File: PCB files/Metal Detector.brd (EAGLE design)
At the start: 100 x 80 mm, 93 parts, among them IC1 NE5534AD, IC2 BQ24133RGYR, IC3 LM317MBSTT3, IC4 ESP32-WROOM-32UE-N4, IC5 CP2102, IC6 LM317MBSTT3, J1 L-KLS1-TSJ3.5-013, Q1 IRF740, Q2 BC556, Q3 SI2312CDS-T1-GE3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

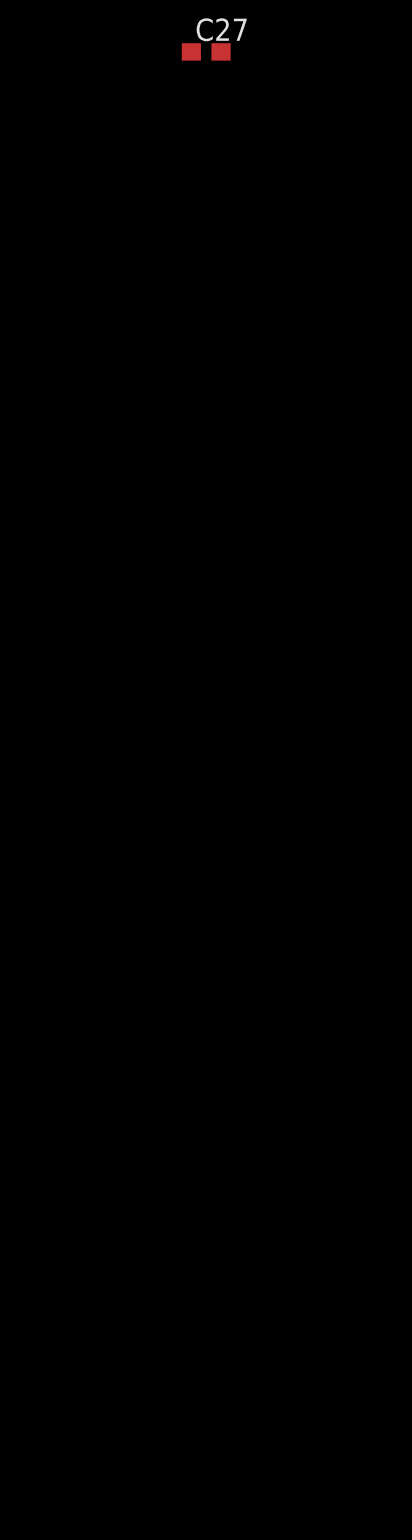
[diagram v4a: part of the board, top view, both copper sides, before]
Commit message: Add files via upload
Still designing battery charge circuit, it is almost over.
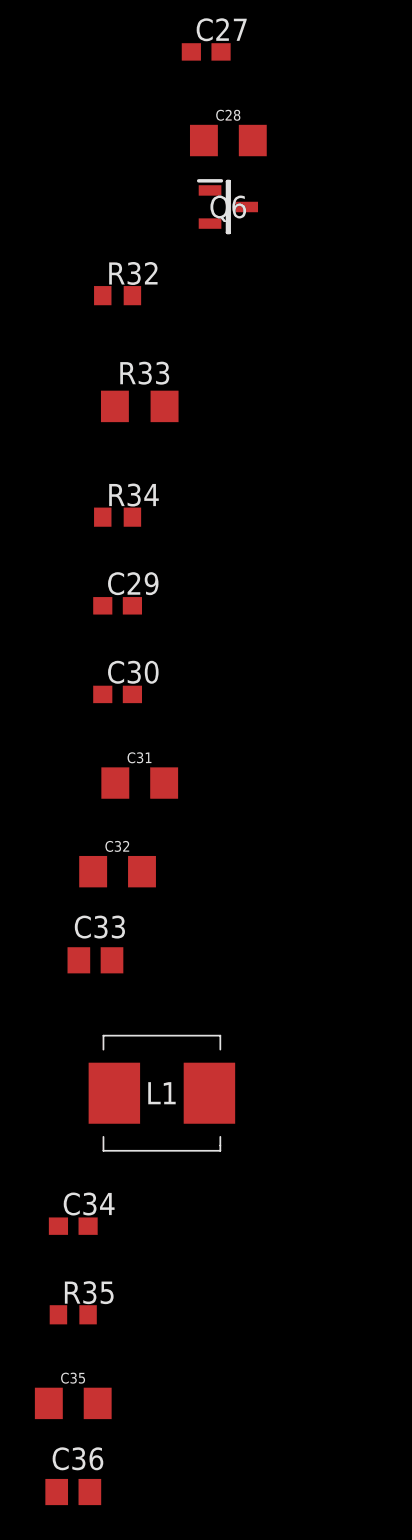
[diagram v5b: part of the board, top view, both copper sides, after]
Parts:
- added C28: 10uF/25 VDC/XR7, SparkFun-Capacitors:1206
- added C29, C30: 0.1uF, rcl:C0603
- added C31, C32, C35: 10uF/25V/XR7, SparkFun-Capacitors:1206
- added C33: 1uF/25V/XR7, rcl:C0805
- added C34: 0.047uF/50V/XR7, rcl:C0603
- added C36: 1uF/16V/XR7, rcl:C0805
- added L1: SRP7028A-3R3M, SRP7028A-3R3M:SRP7028A3R3M
- added Q6: SI2323CDS-T1-GE3, SI2323CDS-T1-GE3:SOT95P237X112-3N
- added R32: 1kΩ, rcl:R0603
- added R33: 0.01RΩ, rcl:R1206
- added R34, R35: 0Ω, rcl:R0603
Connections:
- removed net EXT_PWR_IN: C12.1, C8.1, D10.C, D12.1, D6.C, IC3.3, IC6.3, Q3.3, R15.2, R23.2, X2.2
- removed net PGND_1: IC2.22
- removed net PGND_2: IC2.23
- removed net PVCC_1: IC2.2
- removed net PVCC_2: IC2.3
- removed net SW_1: IC2.1
- removed net SW_2: IC2.24
- new net 12V_IN: D12.1, Q3.3, R15.2, R23.2, X2.2
- new net N$23: Q6.1, R32.1
- new net N$25: C34.2, R35.2
- new net PGND: IC2.22, IC2.23
- new net PVCC: IC2.2, IC2.3
- new net SW: C34.1, IC2.1, IC2.24, L1.1
- net ACP: now also Q5.3; no longer Q5.2
- net BATDRV: now also R32.2
- net BTST: now also R35.1
- net GND: now also C28.2, C30.2, C31.2, C32.2, C33.2, C35.2, C36.1
- net N$21: now also Q5.2; no longer Q5.3
- net N$24: now also C31.1, C32.1, C33.1, Q6.3, R33.2, R34.2; no longer R30.2, R31.2
- net SRN: now also C29.1, R34.1
- net SRP: now also C29.2, C30.1, L1.2, R33.1
- net VCC: now also C12.1, C28.1, C35.1, C8.1, D10.C, D6.C, IC3.3, IC6.3, Q6.2, R30.2, R31.2
- net VREF: now also C36.2

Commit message: Add files via upload
Battery Charge Circuit design process is finished but This design is unexpectedly expencive due to peripheral components.
Founded new IC and will change design for new IC. ( I'm so sorry for that : /) will be more cost effective.
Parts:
- removed C12, C8: 0.1uF, rcl:C075-052X106
- added C37: 1uF/25V/XR7, rcl:C0805
- added C38: 0.1uF/50V/XR7, rcl:C0603
- added C39, C40: 0.1uF, rcl:C2012
- added J2/BATTERY: DG128-5.0-02P-14, DG128-5.0-02P-14:DG1285002P14
- added R36, R37, R38, R39, R40, R41: 0Ω, rcl:R0603
- added R42: 30.1kΩ, rcl:R0603
- added R43: 5.23kΩ, rcl:R0603
- added U$1: 103AP-2, 130-AP2:AT-2_SMI
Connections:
- removed net AGND: IC2.25
- removed net PGND: IC2.22, IC2.23
- removed net VREF: C36.2, IC2.12
- new net N$27: C38.1, R41.2
- net ACSET: now also R38.1, R39.2
- net CELL: now also R40.2
- net GND: now also C37.2, C38.2, C39.2, C40.2, IC2.22, IC2.23, IC2.25, J2/BATTERY.2, R37.1, R39.1, R42.2, U$1.2; no longer C12.2, C8.2
- net ISET: now also R36.1, R37.2
- net N$24: now also J2/BATTERY.1
- net PVCC: now also C28.1, C35.1, Q6.2, R30.2, R31.2
- net REGN: now also C37.1
- net TS: now also R42.1, R43.2, U$1.1
- net TTC: now also R41.1
- net VCC: now also C36.2, C39.1, C40.1, IC2.12, R36.2, R38.2, R40.1, R43.1; no longer C12.1, C28.1, C35.1, C8.1, Q6.2, R30.2, R31.2

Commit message: Add files via upload
Assigned ISET adn ACSET value for selected battery
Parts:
- R36: value 0Ω -> 100kΩ
- R37: value 0Ω -> 12kΩ
- R38: value 0Ω -> 2.2Ω
- R39: value 0Ω -> 4.7Ω
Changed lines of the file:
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@@
 <attribute name="VALUE" x="-140.97" y="-520.7" size="1.27" layer="27"/>
 </element>
-<element name="R36" library="rcl" library_urn="urn:adsk.eagle:library:334" package="R0603" package3d_urn="urn:adsk.eagle:package:23555/3" value="0Ω" x="-140.97" y="-524.51" smashed="yes">
+<element name="R36" library="rcl" library_urn="urn:adsk.eagle:library:334" package="R0603" package3d_urn="urn:adsk.eagle:package:23555/3" value="100kΩ" x="-140.97" y="-524.51" smashed="yes">
 <attribute name="NAME" x="-141.605" y="-523.875" size="1.27" layer="25"/>
 <attribute name="POPULARITY" value="70" x="-140.97" y="-524.51" size="1.778" layer="27" display="off"/>
@@
 <attribute name="VALUE" x="-141.605" y="-526.415" size="1.27" layer="27"/>
 </element>
-<element name="R37" library="rcl" library_urn="urn:adsk.eagle:library:334" package="R0603" package3d_urn="urn:adsk.eagle:package:23555/3" value="0Ω" x="-140.97" y="-529.59" smashed="yes">
+<element name="R37" library="rcl" library_urn="urn:adsk.eagle:library:334" package="R0603" package3d_urn="urn:adsk.eagle:package:23555/3" value="12kΩ" x="-140.97" y="-529.59" smashed="yes">
 <attribute name="NAME" x="-141.605" y="-528.955" size="1.27" layer="25"/>
 <attribute name="POPULARITY" value="70" x="-140.97" y="-529.59" size="1.778" layer="27" display="off"/>
@@
 <attribute name="VALUE" x="-141.605" y="-531.495" size="1.27" layer="27"/>
 </element>
-<element name="R38" library="rcl" library_urn="urn:adsk.eagle:library:334" package="R0603" package3d_urn="urn:adsk.eagle:package:23555/3" value="0Ω" x="-140.97" y="-534.67" smashed="yes">
+<element name="R38" library="rcl" library_urn="urn:adsk.eagle:library:334" package="R0603" package3d_urn="urn:adsk.eagle:package:23555/3" value="2.2Ω" x="-140.97" y="-534.67" smashed="yes">
 <attribute name="NAME" x="-141.605" y="-534.035" size="1.27" layer="25"/>
 <attribute name="POPULARITY" value="70" x="-140.97" y="-534.67" size="1.778" layer="27" display="off"/>
@@
 <attribute name="VALUE" x="-141.605" y="-536.575" size="1.27" layer="27"/>
 </element>
-<element name="R39" library="rcl" library_urn="urn:adsk.eagle:library:334" package="R0603" package3d_urn="urn:adsk.eagle:package:23555/3" value="0Ω" x="-140.97" y="-539.75" smashed="yes">
+<element name="R39" library="rcl" library_urn="urn:adsk.eagle:library:334" package="R0603" package3d_urn="urn:adsk.eagle:package:23555/3" value="4.7Ω" x="-140.97" y="-539.75" smashed="yes">
 <attribute name="NAME" x="-141.605" y="-539.115" size="1.27" layer="25"/>
 <attribute name="POPULARITY" value="70" x="-140.97" y="-539.75" size="1.778" layer="27" display="off"/>

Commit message: Add files via upload
Added LCD connections
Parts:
- added R44: PC16S, piher:PC16S
- DS1: value NHD-12864WG-BTGH-T#N -> WG12864B-TFH-V#N
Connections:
- new net N$28: DS1.3, R44.1S
- net GND: now also DS1.2, DS1.20, R44.1E
- net IO18: now also DS1.17
- net IO22: now also DS1.14
- net IO23: now also DS1.15
- net IO5: now also DS1.16
- net VCC: now also DS1.1, DS1.19, R44.1A
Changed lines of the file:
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@@
 <attribute name="VALUE" x="-59.69" y="-82.55" size="1.778" layer="27" ratio="5" rot="R90"/>
 </element>
-<element name="DS1" library="NHD-12864WG-BTGH-T#N" package="NHD12864WGBTGHTN" value="NHD-12864WG-BTGH-T#N" x="-64.77" y="-153.67" smashed="yes">
+<element name="DS1" library="NHD-12864WG-BTGH-T#N" package="NHD12864WGBTGHTN" value="WG12864B-TFH-V#N" x="-64.77" y="-153.67" smashed="yes">
 <attribute name="ARROW_PART_NUMBER" value="" x="-64.77" y="-153.67" size="1.778" layer="27" display="off"/>
 <attribute name="ARROW_PRICE-STOCK" value="" x="-64.77" y="-153.67" size="1.778" layer="27" display="off"/>
@@
 <attribute name="SPICEPREFIX" value="C" x="-142.24" y="-603.25" size="1.778" layer="27" display="off"/>
 <attribute name="VALUE" x="-143.51" y="-605.79" size="1.27" layer="27"/>
+</element>
+<element name="R44" library="piher" library_urn="urn:adsk.eagle:library:324" package="PC16S" package3d_urn="urn:adsk.eagle:package:22243/1" value="PC16S" x="-154.94" y="-560.07" smashed="yes">
+<attribute name="MF" value="" x="-154.94" y="-560.07" size="1.778" layer="27" display="off"/>
+<attribute name="MPN" value="" x="-154.94" y="-560.07" size="1.778" layer="27" display="off"/>
+<attribute name="NAME" x="-163.26" y="-559.55" size="1.27" layer="25" rot="R90"/>
+<attribute name="OC_FARNELL" value="4452940" x="-154.94" y="-560.07" size="1.778" layer="27" display="off"/>
+<attribute name="OC_NEWARK" value="unknown" x="-154.94" y="-560.07" size="1.778" layer="27" display="off"/>
+<attribute name="POPULARITY" value="4" x="-154.94" y="-560.07" size="1.778" layer="27" display="off"/>
+<attribute name="VALUE" x="-145.04" y="-559.55" size="1.27" layer="27" rot="R90"/>
 </element>
 </elements>
@@
 <contactref element="C39" pad="2"/>
 <contactref element="C40" pad="2"/>
+<contactref element="DS1" pad="20"/>
+<contactref element="DS1" pad="2"/>
+<contactref element="R44" pad="1E"/>
 <wire x1="-119.06" y1="-351.79" x2="-125.31" y2="-381" width="0" layer="19" extent="1-1"/>
 <wire x1="-123.9" y1="-335.28" x2="-119.06" y2="-351.79" width="0" layer="19" extent="1-1"/>
@@
 <wire x1="-141.82" y1="-529.59" x2="-140.65" y2="-518.16" width="0" layer="19" extent="1-1"/>
 <wire x1="-141.82" y1="-539.75" x2="-141.82" y2="-529.59" width="0" layer="19" extent="1-1"/>
-<wire x1="-133.43" y1="-553.72" x2="-141.82" y2="-539.75" width="0" layer="19" extent="1-1"/>
-<wire x1="-141.29" y1="-563.88" x2="-133.43" y2="-553.72" width="0" layer="19" extent="1-1"/>
+<wire x1="-149.94" y1="-553.57" x2="-141.82" y2="-539.75" width="0" layer="19" extent="1-1"/>
+<wire x1="-141.29" y1="-563.88" x2="-149.94" y2="-553.57" width="0" layer="19" extent="1-1"/>
 <wire x1="-141.39" y1="-570.23" x2="-141.29" y2="-563.88" width="0" layer="19" extent="1-1"/>
 <wire x1="-141.39" y1="-580.39" x2="-141.39" y2="-570.23" width="0" layer="19" extent="1-1"/>
+<wire x1="-133.43" y1="-553.72" x2="-141.29" y2="-563.88" width="0" layer="19" extent="1-1"/>
 <wire x1="-138.43" y1="-593.09" x2="-141.39" y2="-580.39" width="0" layer="19" extent="1-1"/>
 <wire x1="-141.39" y1="-598.17" x2="-138.43" y2="-593.09" width="0" layer="19" extent="1-1"/>
 <wire x1="-141.39" y1="-603.25" x2="-141.39" y2="-598.17" width="0" layer="19" extent="1-1"/>
-<wire x1="-73.66" y1="-79.5528" x2="-119.25" y2="-259.08" width="0" layer="19" extent="1-1"/>
+<wire x1="-62.23" y1="-153.67" x2="-119.25" y2="-259.08" width="0" layer="19" extent="1-1"/>
+<wire x1="-16.51" y1="-153.67" x2="-62.23" y2="-153.67" width="0" layer="19" extent="1-1"/>
+<wire x1="-73.66" y1="-79.5528" x2="-62.23" y2="-153.67" width="0" layer="19" extent="1-1"/>
 <wire x1="-68.6562" y1="-76.5556" x2="-73.66" y2="-79.5528" width="0" layer="19" extent="1-1"/>
 <wire x1="-69.85" y1="-64.77" x2="-68.6562" y2="-76.5556" width="0" layer="19" extent="1-1"/>
@@
 <contactref element="C39" pad="1"/>
 <contactref element="C40" pad="1"/>
+<contactref element="DS1" pad="1"/>
+<contactref element="DS1" pad="19"/>
+<contactref element="R44" pad="1A"/>
 <wire x1="-143.09" y1="-598.17" x2="-143.09" y2="-603.25" width="0" layer="19" extent="1-1"/>
 <wire x1="-143.09" y1="-585.47" x2="-143.09" y2="-598.17" width="0" layer="19" extent="1-1"/>
-<wire x1="-141.82" y1="-544.83" x2="-143.09" y2="-585.47" width="0" layer="19" extent="1-1"/>
+<wire x1="-159.94" y1="-553.57" x2="-143.09" y2="-585.47" width="0" layer="19" extent="1-1"/>
+<wire x1="-141.82" y1="-544.83" x2="-159.94" y2="-553.57" width="0" layer="19" extent="1-1"/>
 <wire x1="-140.12" y1="-534.67" x2="-141.82" y2="-544.83" width="0" layer="19" extent="1-1"/>
 <wire x1="-140.12" y1="-524.51" x2="-140.12" y2="-534.67" width="0" layer="19" extent="1-1"/>
@@
 <wire x1="-111.76" y1="-292.1" x2="-114.3" y2="-292.1" width="0" layer="19" extent="1-1"/>
 <wire x1="-116.13" y1="-274.32" x2="-121.92" y2="-280.06" width="0" layer="19" extent="1-1"/>
-<wire x1="-67.125" y1="-65.52" x2="-116.13" y2="-274.32" width="0" layer="19" extent="1-1"/>
+<wire x1="-64.77" y1="-153.67" x2="-116.13" y2="-274.32" width="0" layer="19" extent="1-1"/>
+<wire x1="-19.05" y1="-153.67" x2="-64.77" y2="-153.67" width="0" layer="19" extent="1-1"/>
+<wire x1="-67.125" y1="-65.52" x2="-64.77" y2="-153.67" width="0" layer="19" extent="1-1"/>
 <wire x1="-64.64" y1="-55.88" x2="-67.125" y2="-65.52" width="0" layer="19" extent="1-1"/>
 <wire x1="-63.92" y1="-50.8" x2="-64.64" y2="-55.88" width="0" layer="19" extent="1-1"/>
@@
 <signal name="IO22">
 <contactref element="IC4" pad="36"/>
+<contactref element="DS1" pad="14"/>
+<wire x1="-54.75" y1="-15.72" x2="-31.75" y2="-153.67" width="0" layer="19" extent="1-1"/>
 </signal>
 <signal name="TXD0">
@@
 <contactref element="IC4" pad="32"/>
 <contactref element="IC4" pad="37"/>
+<contactref element="DS1" pad="15"/>
+<wire x1="-54.75" y1="-20.8" x2="-29.21" y2="-153.67" width="0" layer="19" extent="1-1"/>
 <wire x1="-54.75" y1="-14.45" x2="-54.75" y2="-20.8" width="0" layer="19" extent="1-1"/>
 </signal>
@@
 <signal name="IO18">
 <contactref element="IC4" pad="30"/>
+<contactref element="DS1" pad="17"/>
+<wire x1="-54.75" y1="-23.34" x2="-24.13" y2="-153.67" width="0" layer="19" extent="1-1"/>
 </signal>
 <signal name="IO5">
 <contactref element="IC4" pad="29"/>
+<contactref element="DS1" pad="16"/>
+<wire x1="-54.75" y1="-24.61" x2="-26.67" y2="-153.67" width="0" layer="19" extent="1-1"/>
 </signal>
 <signal name="IO17">
@@
 <wire x1="-143.09" y1="-570.23" x2="-141.39" y2="-575.31" width="0" layer="19" extent="1-1"/>
 </signal>
+<signal name="N$28">
+<contactref element="DS1" pad="3"/>
+<contactref element="R44" pad="1S"/>
+<wire x1="-154.94" y1="-553.57" x2="-59.69" y2="-153.67" width="0" layer="19" extent="1-1"/>
+</signal>
 </signals>
